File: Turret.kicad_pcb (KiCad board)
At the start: 2 copper layers, 104 x 54 mm, 25 parts, among them J1 Conn_01x04_Pin, J10 Conn_01x02_Pin, J12 Conn_01x02_Pin, J13 Conn_01x04_Pin, J14 Conn_01x04_Pin, J15 Conn_01x08_Pin, J2 Conn_01x02_Pin, J20 Conn_01x02_Pin, J21 Conn_01x02_Pin, J3 Conn_01x02_Pin, J4 Conn_01x02_Pin, J5 Conn_01x04_Pin, J6 Conn_01x02_Pin, J7 Conn_01x02_Pin, J8 Conn_01x02_Pin, J9 Conn_01x02_Pin

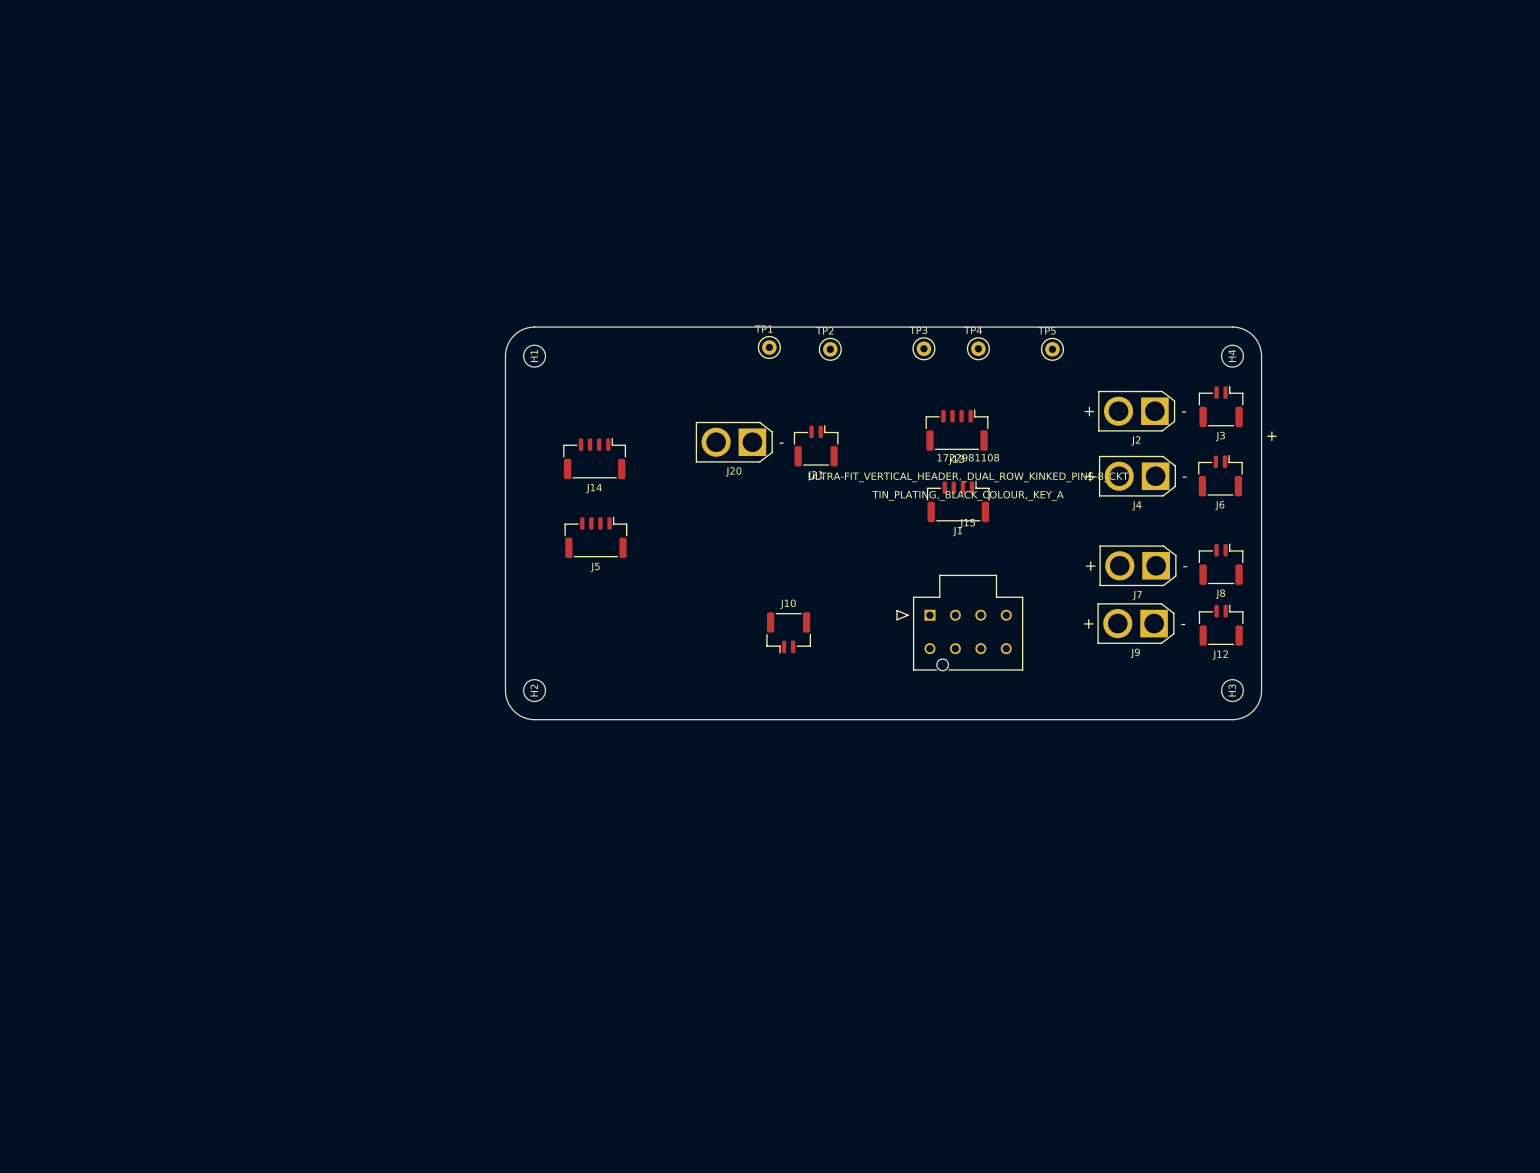
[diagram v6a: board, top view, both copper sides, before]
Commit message: Initial layout of footprints on pcb (not final)
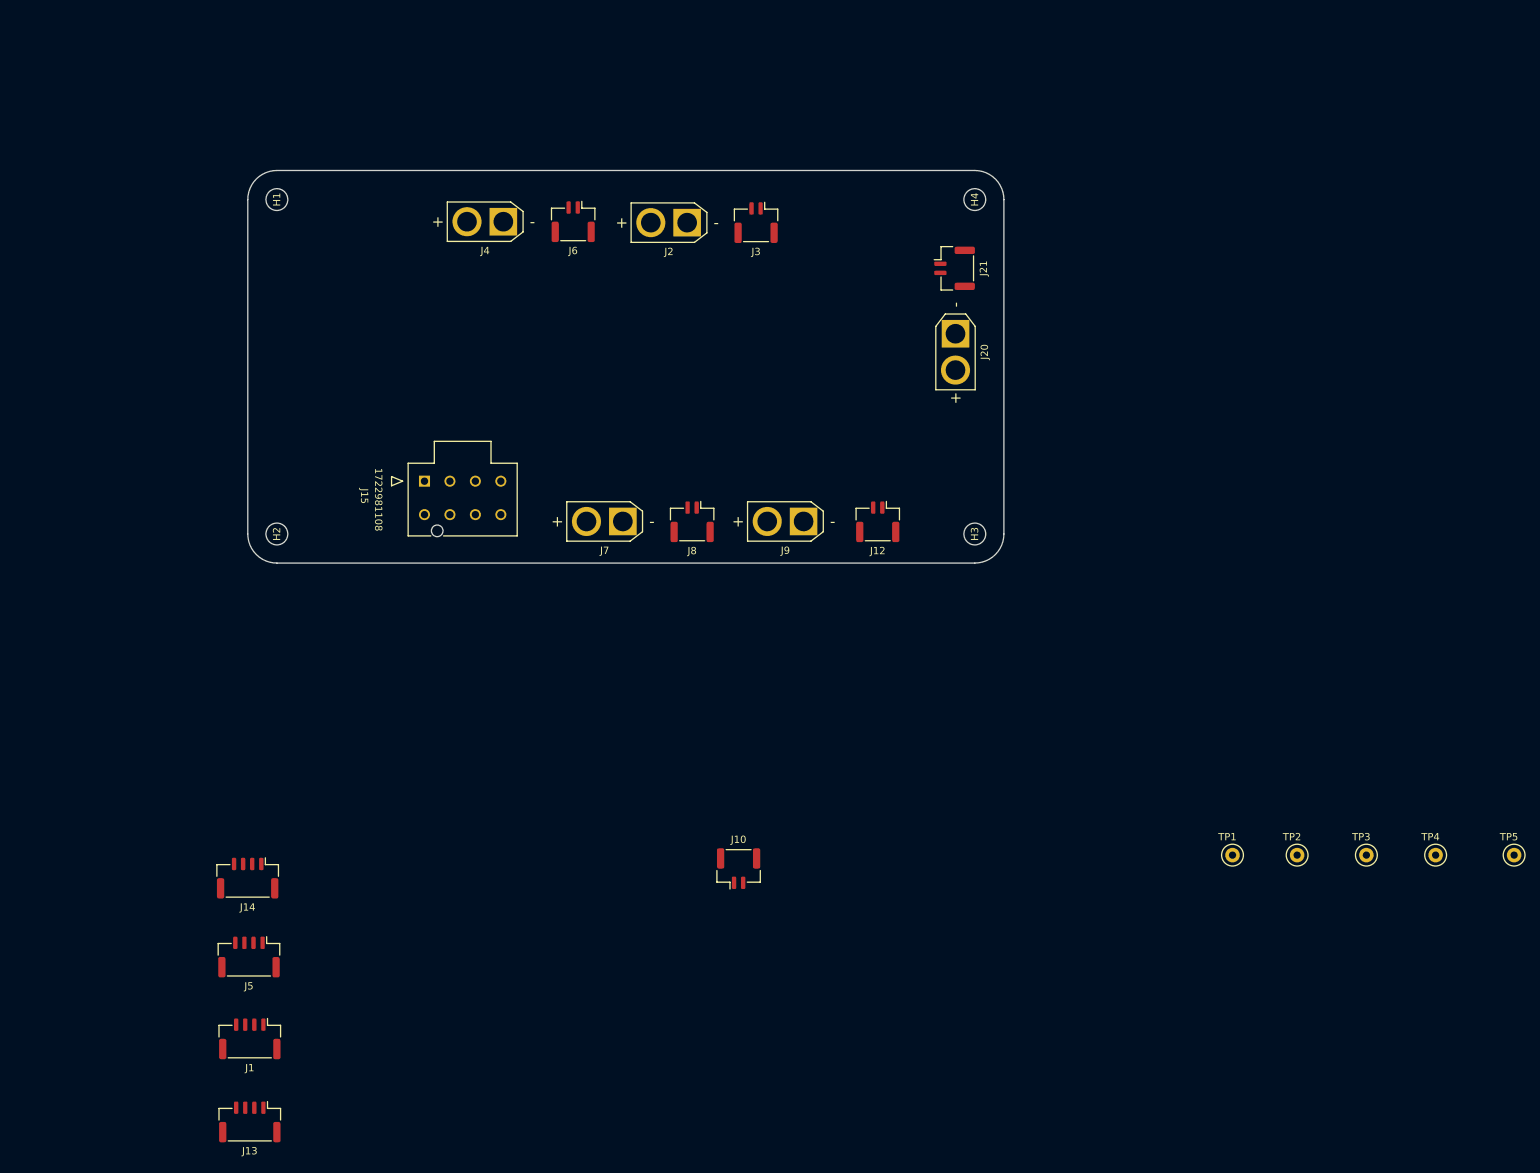
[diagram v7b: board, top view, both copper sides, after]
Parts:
- moved J13 136.1 mm to (40.7, 165.0)
- moved J1 122.3 mm to (40.7, 153.5)
- moved J4 96.3 mm to (75.6, 41.1)
- moved J6 95.6 mm to (85.2, 41.1)
- moved TP2 94.7 mm to (184.8, 128.3)
- moved TP1 94.5 mm to (175.9, 128.3)
- moved TP5 94.2 mm to (214.6, 128.3)
- moved TP4 93.8 mm to (203.8, 128.3)
- moved TP3 92.5 mm to (194.3, 128.3)
- moved J14 74.9 mm to (40.4, 131.4)
- moved J5 74.9 mm to (40.6, 142.3)
- moved J7 73.6 mm to (92.0, 82.4)
- moved J8 73.0 mm to (101.6, 82.4)
- moved J15 71.9 mm to (64.8, 76.8)
- moved J2 69.4 mm to (100.9, 41.3)
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
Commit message: Fixed net names in schematic, initial pcb layout
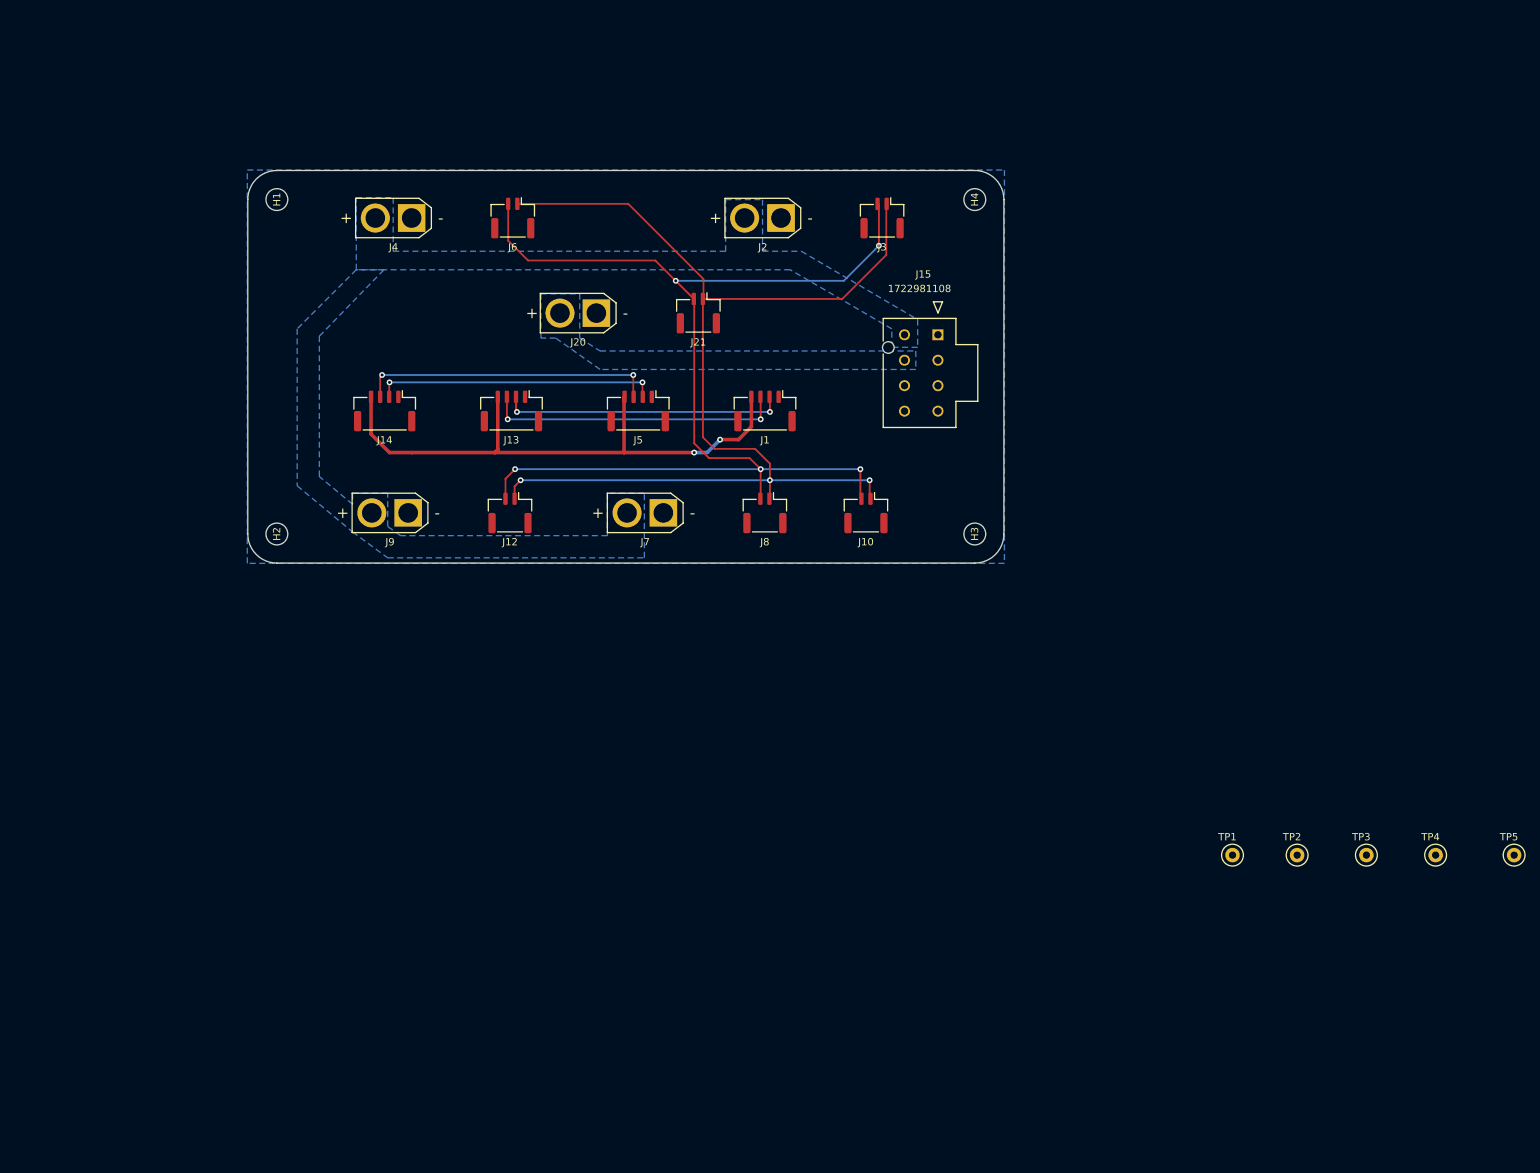
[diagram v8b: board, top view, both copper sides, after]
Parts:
- moved J1 111.7 mm to (111.6, 67.2)
- moved J13 104.2 mm to (76.7, 67.2)
- moved J5 92.2 mm to (94.2, 67.2)
- moved J15 73.4 mm to (135.4, 56.7), turned to -90 degrees
- moved J14 67.0 mm to (59.3, 67.2)
- moved J9 54.4 mm to (62.5, 81.2)
- moved J10 52.0 mm to (125.5, 81.2), turned to 180 degrees
- moved J12 50.6 mm to (76.5, 81.2)
- moved J20 49.5 mm to (88.4, 53.7), turned to 180 degrees
- moved J21 35.8 mm to (102.4, 53.7), turned to 180 degrees
- moved J3 17.3 mm to (127.7, 40.6)
- moved J2 12.9 mm to (113.8, 40.6)
- moved J4 12.6 mm to (63.0, 40.6)
- moved J8 10.1 mm to (111.6, 81.2)
- moved J6 8.33 mm to (76.9, 40.6)
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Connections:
- J2 pad 2: /+24V Shooter -> /+24V_Shooter
- J20 pad 2: /+24V Gimbal -> /+24V_Gimbal
- J4 pad 2: /+24V Shooter -> /+24V_Shooter
- J7 pad 2: /+24V Shooter -> /+24V_Shooter
- J9 pad 2: /+24V Shooter -> /+24V_Shooter
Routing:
- net /CANH: track 0.00 -> 160.5 mm, vias 0 -> 5
- net /CANL: track 0.00 -> 155.5 mm, vias 0 -> 3
- net +3.3V: track 0.00 -> 79.6 mm, vias 0 -> 2
- net /UART_RX: track 0.00 -> 41.0 mm, vias 0 -> 2
- net /SWCLK: track 0.00 -> 40.7 mm, vias 0 -> 2
- net /UART_TX: track 0.00 -> 39.0 mm, vias 0 -> 2
- net /SWDIO: track 0.00 -> 38.8 mm, vias 0 -> 2
- added copper zone on B.Cu, net /+24V_Gimbal
- added copper zone on B.Cu, net /+24V_Shooter
- added copper zone on B.Cu, net GND
